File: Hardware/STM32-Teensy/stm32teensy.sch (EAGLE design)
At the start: 25 parts, among them U1 STM32F413CGU3, U2 AP2112K-3.3TRG1, Y1 CRYSTAL-3.2X2.54-PIN

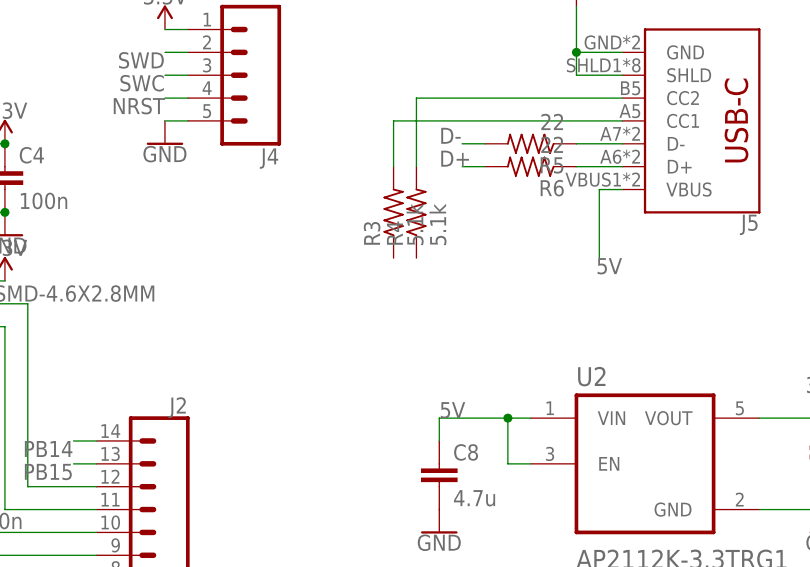
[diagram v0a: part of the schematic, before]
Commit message: ibooster v2, stm32teensy work
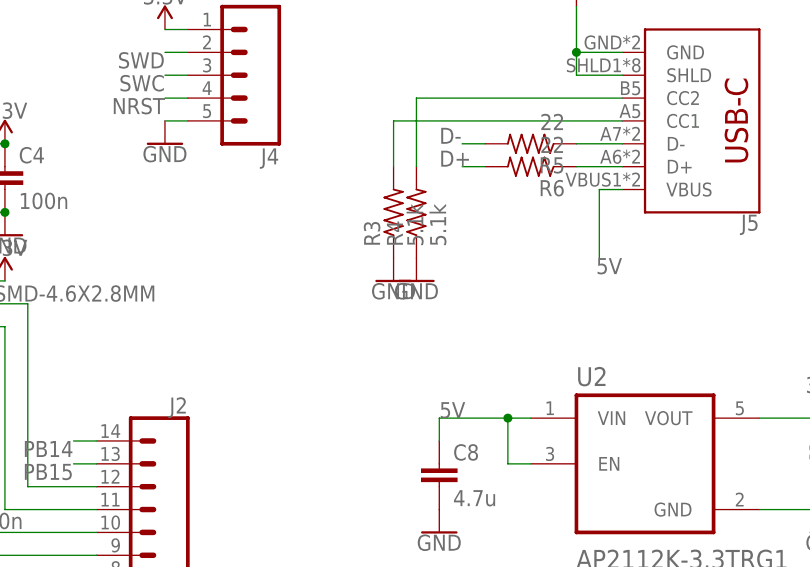
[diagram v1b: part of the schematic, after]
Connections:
- net GND: now also R3.1, R4.1
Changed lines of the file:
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@@
 <part name="GND13" library="SparkFun-PowerSymbols" library_urn="urn:adsk.eagle:library:530" deviceset="GND" device=""/>
 <part name="SUPPLY9" library="SparkFun-PowerSymbols" library_urn="urn:adsk.eagle:library:530" deviceset="3.3V" device=""/>
+<part name="GND14" library="SparkFun-PowerSymbols" library_urn="urn:adsk.eagle:library:530" deviceset="GND" device=""/>
+<part name="GND15" library="SparkFun-PowerSymbols" library_urn="urn:adsk.eagle:library:530" deviceset="GND" device=""/>
 </parts>
 <sheets>
@@
 <instance part="SUPPLY9" gate="G$1" x="142.24" y="58.42" smashed="yes">
 <attribute name="VALUE" x="142.24" y="61.214" size="1.778" layer="96" align="bottom-center"/>
+</instance>
+<instance part="GND14" gate="1" x="93.98" y="73.66" smashed="yes">
+<attribute name="VALUE" x="93.98" y="73.406" size="1.778" layer="96" align="top-center"/>
+</instance>
+<instance part="GND15" gate="1" x="96.52" y="73.66" smashed="yes">
+<attribute name="VALUE" x="96.52" y="73.406" size="1.778" layer="96" align="top-center"/>
 </instance>
 </instances>
@@
 <junction x="142.24" y="48.26"/>
 </segment>
+<segment>
+<pinref part="R3" gate="G$1" pin="1"/>
+<pinref part="GND14" gate="1" pin="GND"/>
+</segment>
+<segment>
+<pinref part="R4" gate="G$1" pin="1"/>
+<pinref part="GND15" gate="1" pin="GND"/>
+</segment>
 </net>
